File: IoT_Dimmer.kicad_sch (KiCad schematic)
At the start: 0 parts

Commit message: add lib
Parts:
- added C1: 0.05uF, symbol Device:C
- added C2: 0.01uF, symbol Device:C
- added D1: BTA204S-800, symbol Triac_Thyristor:Generic_Triac_A1A2G
- added J1, J2: Screw_Terminal_01x02, symbol Connector:Screw_Terminal_01x02
- added PS1: IRM-02-3.3, Converter_ACDC:Converter_ACDC_MeanWell_IRM-02-xx_THT, symbol Converter_ACDC:IRM-02-3.3
- added R1: 360, symbol Device:R
- added R2: 470, symbol Device:R
- added R3: 39, symbol Device:R
- added U1: MOC3021M, symbol Relay_SolidState:MOC3021M
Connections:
- new net: R1.1, U1.6
- new net: C1.1, R1.2, R2.1
- new net: D1.2 (A2), R2.2, R3.1
- new net: C2.1, R3.2
- new net: C1.2, C2.2, D1.1 (A1)
- new net: D1.3 (G), U1.4
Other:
- company: (none) -> No
- title: (none) -> IoT Dimmer

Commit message: CPU and 220
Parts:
- added AE1: Antenna, symbol Device:Antenna
- added C3, C4: C, symbol Device:C
- added C5, C6: 10pF, symbol Device:C
- added C7, C8: 0.1uF, symbol Device:C
- added J3: Conn_01x06_Pin, symbol Connector:Conn_01x06_Pin
- added L1: L, symbol Device:L
- added R4, R5: 33k, symbol Device:R
- added R6, R7, R8: 10k, symbol Device:R
- added R9: 500, symbol Device:R
- added TP1, TP2: ResetPoint, symbol Connector:TestPoint_2Pole
- added U2: VOS628AT, VOS628AT:SOIC127P700X210-4N, symbol VOS628AT:VOS628AT
- added U3: ESP32-C6FH4, Package_DFN_QFN:QFN-32-1EP_5x5mm_P0.5mm_EP3.6x3.6mm, symbol PCM_Espressif:ESP32-C6FH4
- added Y2: Crystal_GND24, symbol Device:Crystal_GND24
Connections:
- net at PS1.1 (AC/N): now also D1.2 (A2), J2.1 (Pin_1), R2.2, R3.1, R5.2
- net at PS1.2 (AC/L): now also J1.1 (Pin_1), J2.2 (Pin_2), R4.2
- net at C1.2, C2.2, D1.1 (A1): now also J1.2 (Pin_2)
- new net: R9.1, U3.21 (U0TXD/GPIO16/FSPICS0)
- new net: R4.1, U2.1
- new net: R5.1, U2.2
- new net: R8.1, U3.14 (GPIO8)
- new net: AE1.1 (A), C4.1, L1.1
- new net: C3.1, L1.2, U3.1 (ANT)
- new net: U3.2 (VDDA3P3), U3.3 (VDDA3P3)
- new net +3V3: J3.1 (Pin_1), R6.2, R7.2, R8.2
- new net GND: C3.2, C4.2, C5.2, C6.2, C7.2, C8.2, J3.6 (Pin_6), TP1.1, TP2.1, U3.33 (GND), Y2.2, Y2.4
- new net RX: J3.3 (Pin_3), U3.22 (U0RXD/GPIO17/FSPICS1)
- new net TX: J3.2 (Pin_2), R9.2
- new net boot: C8.1, J3.4 (Pin_4), R7.1, TP2.2, U3.15 (GPIO9)
- new net chip_pu/rst: C7.1, J3.5 (Pin_5), R6.1, TP1.2, U3.4 (CHIP_PU)
- new net xtal_n: C5.1, U3.30 (XTAL_N), Y2.3
- new net xtal_p: C6.1, U3.31 (XTAL_P), Y2.1
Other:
- note added: "220 VAC (HIGH VOLTAGE)"
- moved on the sheet: C1, C2, D1, J1, J2, PS1, R1, R2, R3, U1

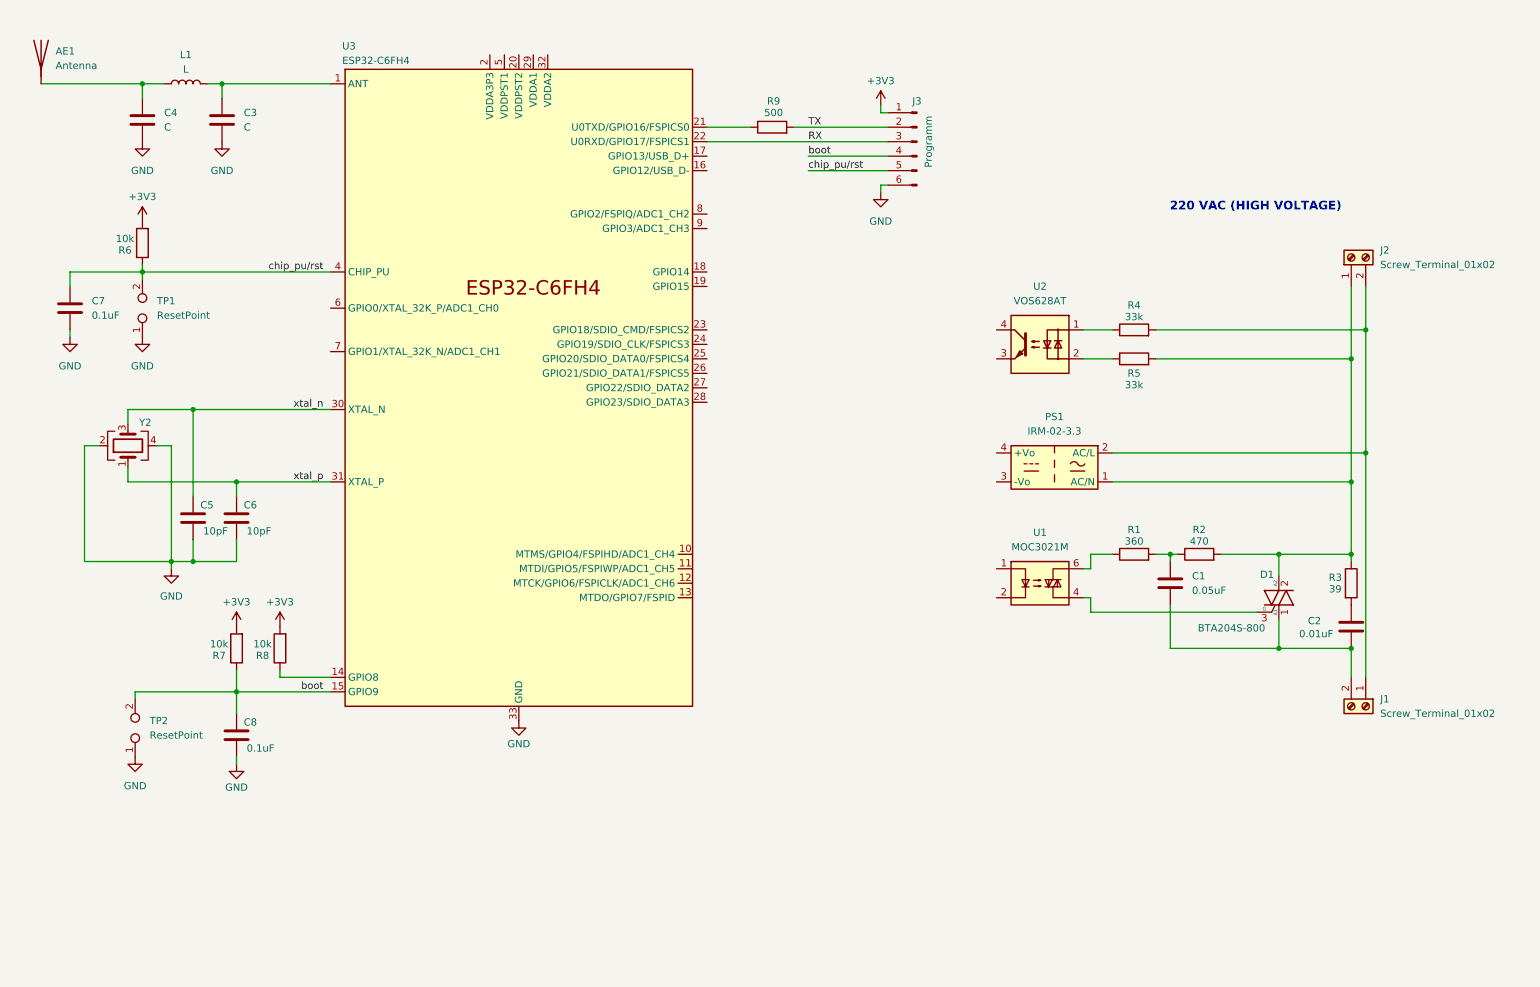
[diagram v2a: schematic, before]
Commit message: Power esp32
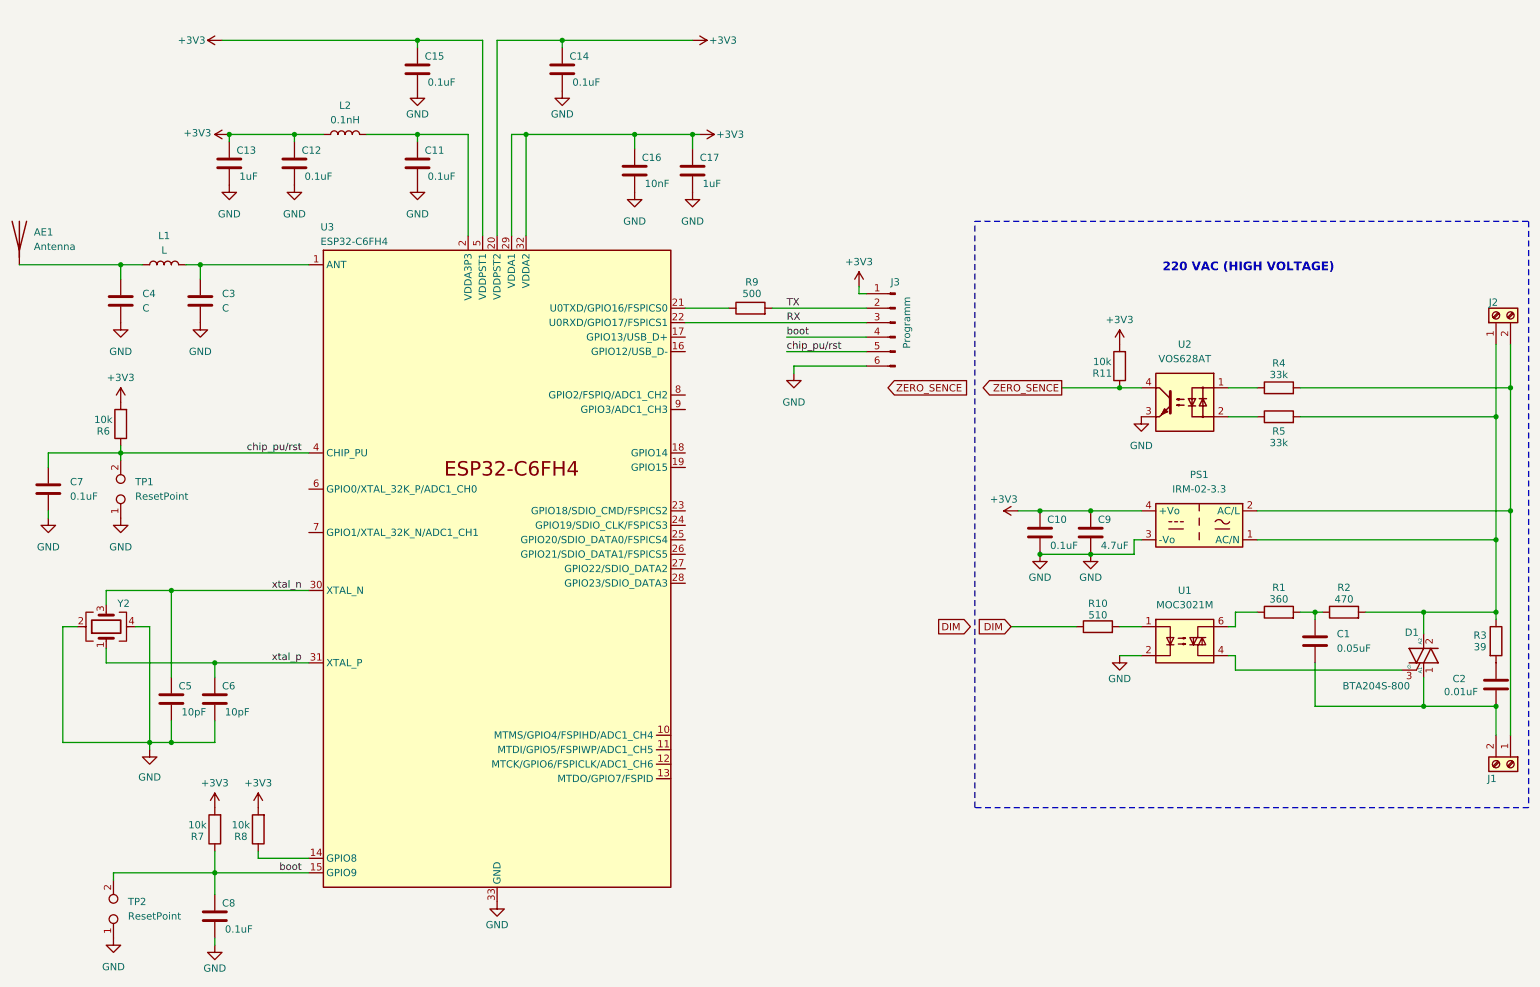
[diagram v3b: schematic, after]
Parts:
- added C10, C11, C12, C14, C15: 0.1uF, symbol Device:C
- added C13, C17: 1uF, symbol Device:C
- added C16: 10nF, symbol Device:C
- added C9: 4.7uF, symbol Device:C
- added L2: 0.1nH, symbol Device:L
- added R10: 510, symbol Device:R
- added R11: 10k, symbol Device:R
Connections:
- net +3V3: now also PS1.4 (+Vo), U3.20 (VDDPST2), U3.29 (VDDA1), U3.32 (VDDA2), U3.5 (VDDPST1), C10.1, C12.1, C13.1, C14.1, C15.1, C16.1, C17.1, C9.1, L2.1, R11.2
- net GND: now also PS1.3 (-Vo), U1.2, U2.3, C10.2, C11.2, C12.2, C13.2, C14.2, C15.2, C16.2, C17.2, C9.2
- net ZERO_SENCE: now reaches U2.4
- net ZERO_SENCE: now also R11.1
- net at U1.1: now also R10.2
- net at U3.2 (VDDA3P3), U3.3 (VDDA3P3): now also C11.1, L2.2
- new net DIM: R10.1
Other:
- moved on the sheet: AE1, C1, C2, C3, C4, C5, C6, C7, C8, D1, J1, J2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

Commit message: beta sheet
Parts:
- added C18, C19, C20, C21: 0.1uF, symbol Device:C
- added F1: 2A, symbol Device:Fuse
- added R12, R13, R14: 10k, Resistor_SMD:R_0805_2012Metric, symbol Device:R
- added RV1: Varistor, Resistor_SMD:R_0805_2012Metric, symbol Device:Varistor
- added SW1: RotaryEncoder_Switch_MP, symbol Device:RotaryEncoder_Switch_MP
- AE1: footprint (none) -> RF_Antenna:Molex_47948-0001_2.4Ghz
- R1, R10, R11, R2, R3, R6, R7, R8, R9: footprint (none) -> Resistor_SMD:R_0805_2012Metric
- TP1: value ResetPoint -> RST; footprint (none) -> TestPoint:TestPoint_Bridge_Pitch2.0mm_Drill0.7mm
- TP2: value ResetPoint -> BOOT; footprint (none) -> TestPoint:TestPoint_Bridge_Pitch2.0mm_Drill0.7mm
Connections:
- net +3V3: now also R12.2, R13.2, R14.2
- net DIM: now also U3.24 (GPIO19/SDIO_CLK/FSPICS3)
- net GND: now also C18.1, C19.2, C20.2, C21.2, SW1.C, SW1.MP, SW1.S2
- net ZERO_SENCE: now also U3.23 (GPIO18/SDIO_CMD/FSPICS2), C21.1
- net at D1.2 (A2), PS1.1 (AC/N), R2.2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: now also F1.2, RV1.2; no longer J2.1 (Pin_1)
- net at J1.1 (Pin_1), J2.2 (Pin_2), PS1.2 (AC/L)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: now also RV1.1
- net ENC_SW: now reaches U3.25 (GPIO20/SDIO_DATA0/FSPICS4)
- net ENC_SW: now also C20.1, R14.1, SW1.S1
- net ENC_A: now reaches U3.26 (GPIO21/SDIO_DATA1/FSPICS5)
- net ENC_A: now also C19.1, R13.1, SW1.A
- net ENC_B: now reaches U3.27 (GPIO22/SDIO_DATA2)
- net ENC_B: now also C18.2, R12.1, SW1.B
- new net: F1.1, J2.1 (Pin_1)
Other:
- note added: "Encoder"
- moved on the sheet: AE1, C1, C10, C11, C12, C13, C14, C15, C16, C17, C2, C3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

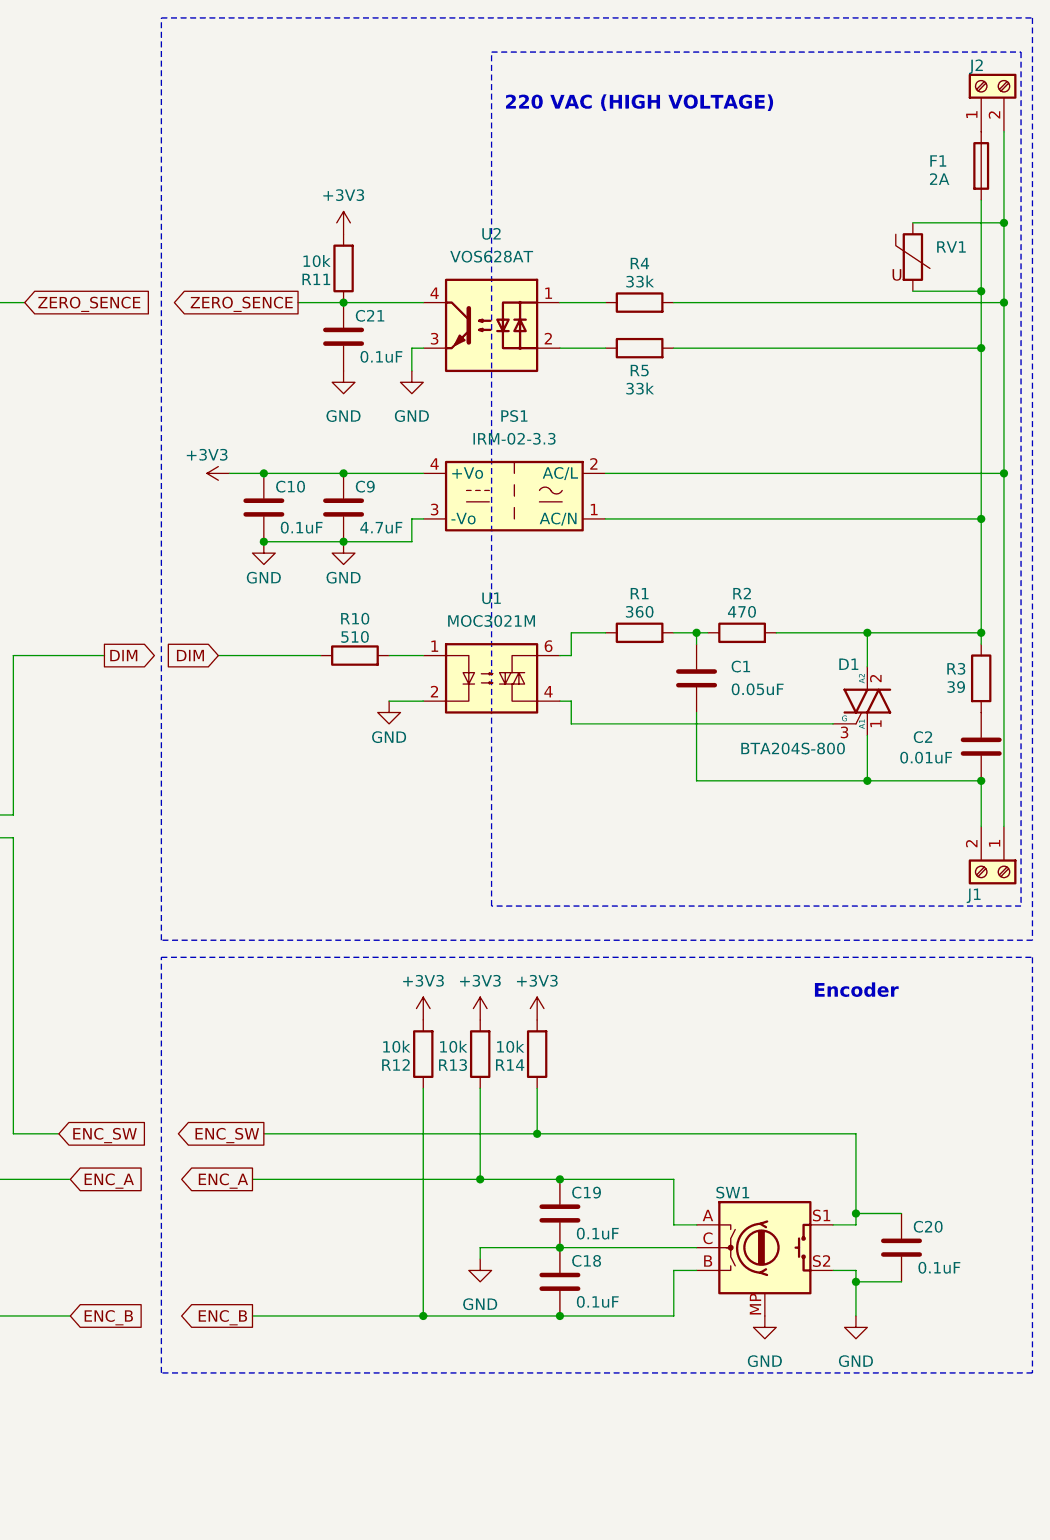
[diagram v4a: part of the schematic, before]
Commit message: Power esp32
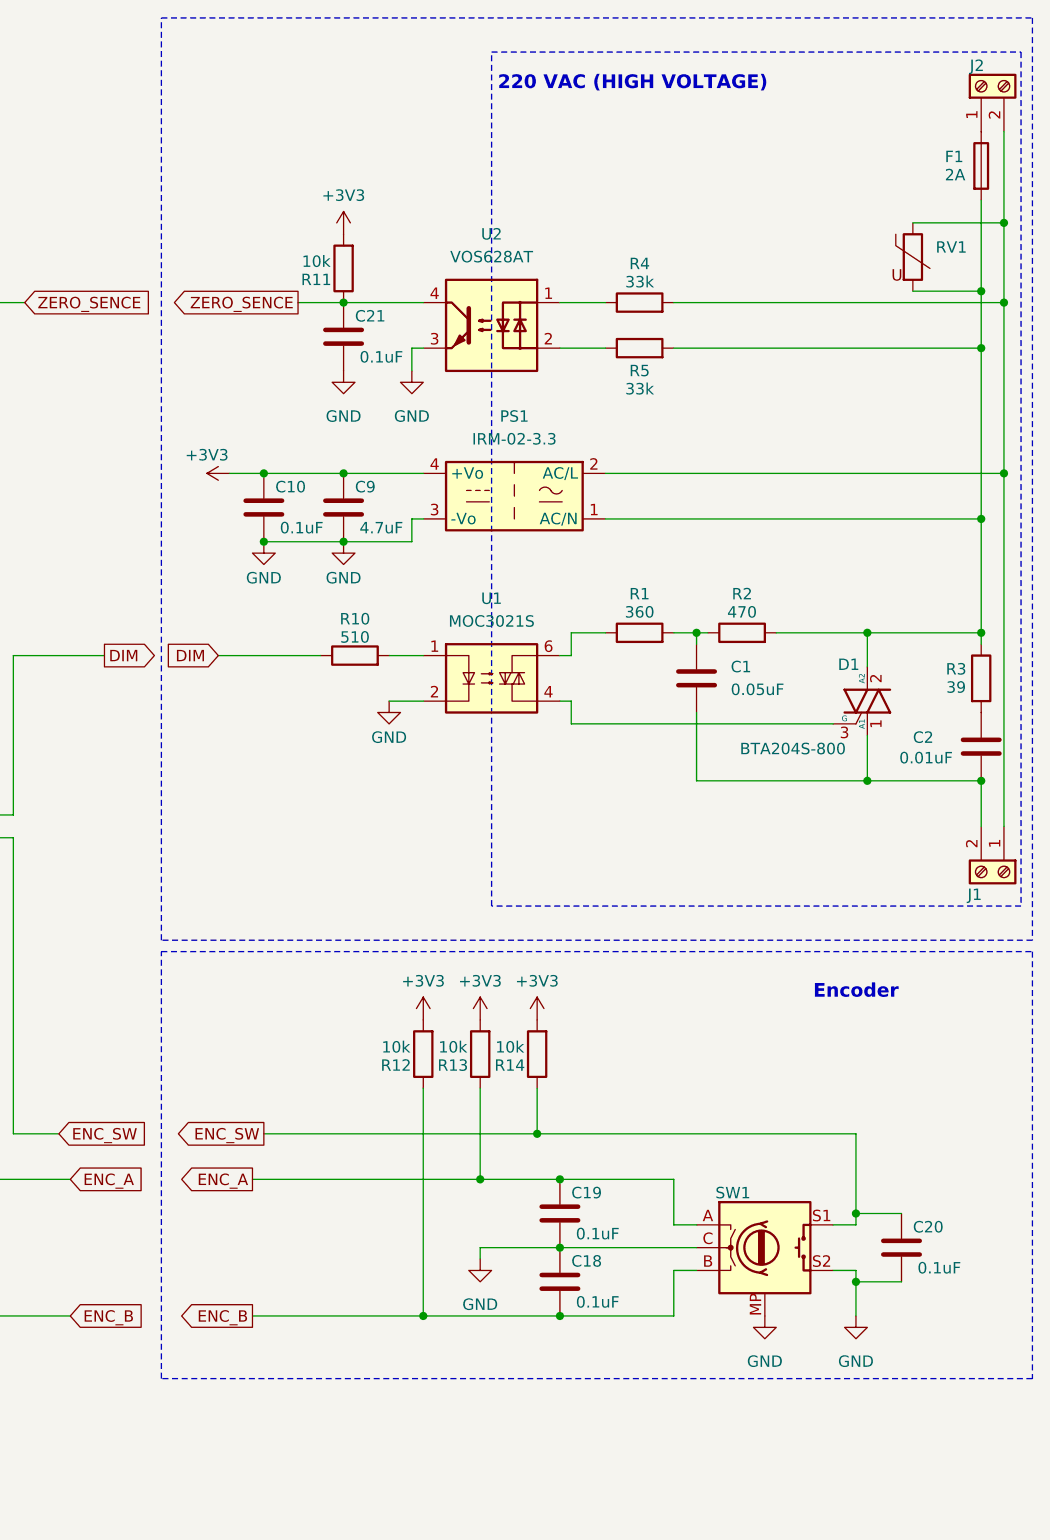
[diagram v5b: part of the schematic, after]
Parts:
- C10, C11, C12, C13, C14, C15, C16, C17, C18, C19, C20, C21, C5, C6, C7, C8, C9: footprint (none) -> Capacitor_SMD:C_0805_2012Metric
- D1: footprint (none) -> Package_TO_SOT_SMD:TO-252-3_TabPin2
- F1: footprint (none) -> Fuse:Fuse_Littelfuse-NANO2-462
- RV1: footprint Resistor_SMD:R_0805_2012Metric -> Varistor:Varistor_Panasonic_VF
- U1: value MOC3021M -> MOC3021S; footprint (none) -> MOC3021SM:DIP6_SMD
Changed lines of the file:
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@@
 	)
 	(rectangle
-		(start 185.42 118.745)
-		(end 282.575 165.1)
+		(start 185.42 118.11)
+		(end 282.575 165.735)
 		(stroke
 			(width 0)
@@
 	(text "220 VAC (HIGH VOLTAGE)"
 		(exclude_from_sim no)
-		(at 238.76 23.622 0)
+		(at 237.998 21.336 0)
 		(effects
 			(font
@@
 			)
 		)
-		(property "Footprint" ""
+		(property "Footprint" "Capacitor_SMD:C_0805_2012Metric"
 			(at 113.9952 26.67 0)
 			(effects
@@
 			)
 		)
-		(property "Footprint" ""
+		(property "Footprint" "Capacitor_SMD:C_0805_2012Metric"
 			(at 206.7052 72.39 0)
 			(effects
@@
 			)
 		)
-		(property "Footprint" ""
+		(property "Footprint" "Capacitor_SMD:C_0805_2012Metric"
 			(at 45.4152 137.16 0)
 			(effects
@@
 		(dnp no)
 		(property "Reference" "F1"
-			(at 271.018 29.972 0)
+			(at 272.796 29.464 0)
 			(effects
 				(font
@@
 		)
 		(property "Value" "2A"
-			(at 271.018 32.004 0)
+			(at 272.796 31.496 0)
 			(effects
 				(font
@@
 			)
 		)
-		(property "Footprint" ""
+		(property "Footprint" "Fuse:Fuse_Littelfuse-NANO2-462"
 			(at 275.082 30.48 90)
 			(effects
@@
 			)
 		)
-		(property "Footprint" ""
+		(property "Footprint" "Capacitor_SMD:C_0805_2012Metric"
 			(at 53.0352 137.16 0)
 			(effects
@@
 			)
 		)
-		(property "Footprint" ""
+		(property "Footprint" "Capacitor_SMD:C_0805_2012Metric"
 			(at 268.9352 154.94 0)
 			(effects
@@
 			)
 		)
-		(property "Footprint" ""
+		(property "Footprint" "Capacitor_SMD:C_0805_2012Metric"
 			(at 55.5752 43.18 0)
 			(effects
@@
 			)
 		)
-		(property "Footprint" ""
+		(property "Footprint" "Capacitor_SMD:C_0805_2012Metric"
 			(at 67.0052 43.18 0)
 			(effects
@@
 			)
 		)
-		(property "Footprint" ""
+		(property "Footprint" "Package_TO_SOT_SMD:TO-252-3_TabPin2"
 			(at 266.065 89.535 90)
 			(effects
@@
 			)
 		)
-		(property "Value" "MOC3021M"
+		(property "Value" "MOC3021S"
 			(at 222.25 81.28 0)
 			(effects
@@
 			)
 		)
-		(property "Footprint" ""
+		(property "Footprint" "MOC3021SM:DIP6_SMD"
 			(at 217.17 92.71 0)
 			(effects
@@
 			)
 		)
-		(property "Footprint" ""
+		(property "Footprint" "Capacitor_SMD:C_0805_2012Metric"
 			(at 88.5952 26.67 0)
 			(effects
@@
 			)
 		)
-		(property "Footprint" ""
+		(property "Footprint" "Capacitor_SMD:C_0805_2012Metric"
 			(at 206.7052 53.34 0)
 			(effects
@@
 			)
 		)
-		(property "Footprint" ""
+		(property "Footprint" "Capacitor_SMD:C_0805_2012Metric"
 			(at 230.8352 151.13 0)
 			(effects
@@
 			)
 		)
-		(property "Footprint" ""
+		(property "Footprint" "Capacitor_SMD:C_0805_2012Metric"
 			(at 230.8352 158.75 0)
 			(effects
@@
 			)
 		)
-		(property "Footprint" ""
+		(property "Footprint" "Capacitor_SMD:C_0805_2012Metric"
 			(at 53.0352 175.26 0)
 			(effects
@@
 			)
 		)
-		(property "Footprint" ""
+		(property "Footprint" "Capacitor_SMD:C_0805_2012Metric"
 			(at 136.8552 44.45 0)
 			(effects
@@
 			)
 		)
-		(property "Footprint" ""
+		(property "Footprint" "Capacitor_SMD:C_0805_2012Metric"
 			(at 23.8252 100.33 0)
 			(effects
@@
 			)
 		)
-		(property "Footprint" ""
+		(property "Footprint" "Capacitor_SMD:C_0805_2012Metric"
 			(at 88.5952 43.18 0)
 			(effects
@@
 			)
 		)
-		(property "Footprint" ""
+		(property "Footprint" "Capacitor_SMD:C_0805_2012Metric"
 			(at 126.6952 44.45 0)
 			(effects
@@
 			)
 		)
-		(property "Footprint" "Resistor_SMD:R_0805_2012Metric"
+		(property "Footprint" "Varistor:Varistor_Panasonic_VF"
 			(at 267.462 40.64 90)
 			(effects
@@
 			)
 		)
-		(property "Footprint" ""
+		(property "Footprint" "Capacitor_SMD:C_0805_2012Metric"
 			(at 197.8152 72.39 0)
 			(effects

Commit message: PCB_start
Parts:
- C1: footprint (none) -> Capacitor_SMD:C_1812_4532Metric
- C10, C11, C12, C13, C14, C15, C16, C17, C18, C19, C20, C21, C5, C6, C7, C8, C9: footprint Capacitor_SMD:C_0805_2012Metric -> Capacitor_SMD:C_0603_1608Metric
- C2: value 0.01uF -> 22nF; footprint (none) -> Capacitor_SMD:C_1812_4532Metric
- C3, C4: footprint (none) -> Capacitor_SMD:C_0603_1608Metric
- F1: value 2A -> 3A
- J1: value Screw_Terminal_01x02 -> Wago_2059-302998-403:CONN2_2059-302&slash_998-403_WAG
- J2: footprint (none) -> Wago_2059-302998-403:CONN2_2059-302&slash_998-403_WAG
- L1, L2: footprint (none) -> Inductor_SMD:L_0805_2012Metric
- R1, R2, R3: footprint Resistor_SMD:R_0805_2012Metric -> Resistor_SMD:R_1206_3216Metric
- R10, R11, R12, R13, R14, R6, R7, R8, R9: footprint Resistor_SMD:R_0805_2012Metric -> Resistor_SMD:R_0603_1608Metric
- R4, R5: value 33k -> 75k; footprint (none) -> Resistor_SMD:R_1206_3216Metric
- RV1: footprint Varistor:Varistor_Panasonic_VF -> Varistor:RV_Disc_D7mm_W3.4mm_P5mm
- SW1: value RotaryEncoder_Switch_MP -> EVE-SBBFE516B
- Y2: footprint (none) -> Crystal:Crystal_SMD_2016-4Pin_2.0x1.6mm
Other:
- moved on the sheet: C10, C9, PS1, R2
